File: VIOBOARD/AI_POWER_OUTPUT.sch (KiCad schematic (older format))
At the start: 17 parts, among them J5 24V OUTPUT

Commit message: Libraries modified as part of the BBB cape developement.
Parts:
- D24, D25, D26, D27, D28, D29, D30, D31: symbol device:D_ALT -> VIOBOARD-rescue:D_ALT-device
- R70, R71, R72, R73, R74, R75, R76, R77: symbol device:R -> VIOBOARD-rescue:R-device
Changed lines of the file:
@@
 	3150 4000 3450 4000
 $Comp
-L device:D_ALT D25
+L VIOBOARD-rescue:D_ALT-device D25
 U 1 1 599B8BEA
 P 6950 3600
@@
 $EndComp
 $Comp
-L device:D_ALT D24
+L VIOBOARD-rescue:D_ALT-device D24
 U 1 1 599B8BF2
 P 6950 3400
@@
 $EndComp
 $Comp
-L device:D_ALT D26
+L VIOBOARD-rescue:D_ALT-device D26
 U 1 1 599B9024
 P 6950 3800
@@
 $EndComp
 $Comp
-L device:D_ALT D27
+L VIOBOARD-rescue:D_ALT-device D27
 U 1 1 599B9072
 P 6950 4000
@@
 $EndComp
 $Comp
-L device:D_ALT D28
+L VIOBOARD-rescue:D_ALT-device D28
 U 1 1 599B90AF
 P 6950 4200
@@
 $EndComp
 $Comp
-L device:D_ALT D29
+L VIOBOARD-rescue:D_ALT-device D29
 U 1 1 599B90F1
 P 6950 4400
@@
 $EndComp
 $Comp
-L device:D_ALT D30
+L VIOBOARD-rescue:D_ALT-device D30
 U 1 1 599B9136
 P 6950 4600
@@
 $EndComp
 $Comp
-L device:D_ALT D31
+L VIOBOARD-rescue:D_ALT-device D31
 U 1 1 599B9184
 P 6950 4800
@@
 	7100 4800 8000 4800
 $Comp
-L device:R R70
+L VIOBOARD-rescue:R-device R70
 U 1 1 5A43596E
 P 8150 3400
@@
 $EndComp
 $Comp
-L device:R R71
+L VIOBOARD-rescue:R-device R71
 U 1 1 5A435AC5
 P 8150 3600
@@
 $EndComp
 $Comp
-L device:R R72
+L VIOBOARD-rescue:R-device R72
 U 1 1 5A435B1A
 P 8150 3800
@@
 $EndComp
 $Comp
-L device:R R73
+L VIOBOARD-rescue:R-device R73
 U 1 1 5A435B7A
 P 8150 4000
@@
 $EndComp
 $Comp
-L device:R R74
+L VIOBOARD-rescue:R-device R74
 U 1 1 5A435BDA
 P 8150 4200
@@
 $EndComp
 $Comp
-L device:R R75
+L VIOBOARD-rescue:R-device R75
 U 1 1 5A435C4C
 P 8150 4400
@@
 $EndComp
 $Comp
-L device:R R76
+L VIOBOARD-rescue:R-device R76
 U 1 1 5A435CFC
 P 8150 4600
@@
 $EndComp
 $Comp
-L device:R R77
+L VIOBOARD-rescue:R-device R77
 U 1 1 5A435D60
 P 8150 4800

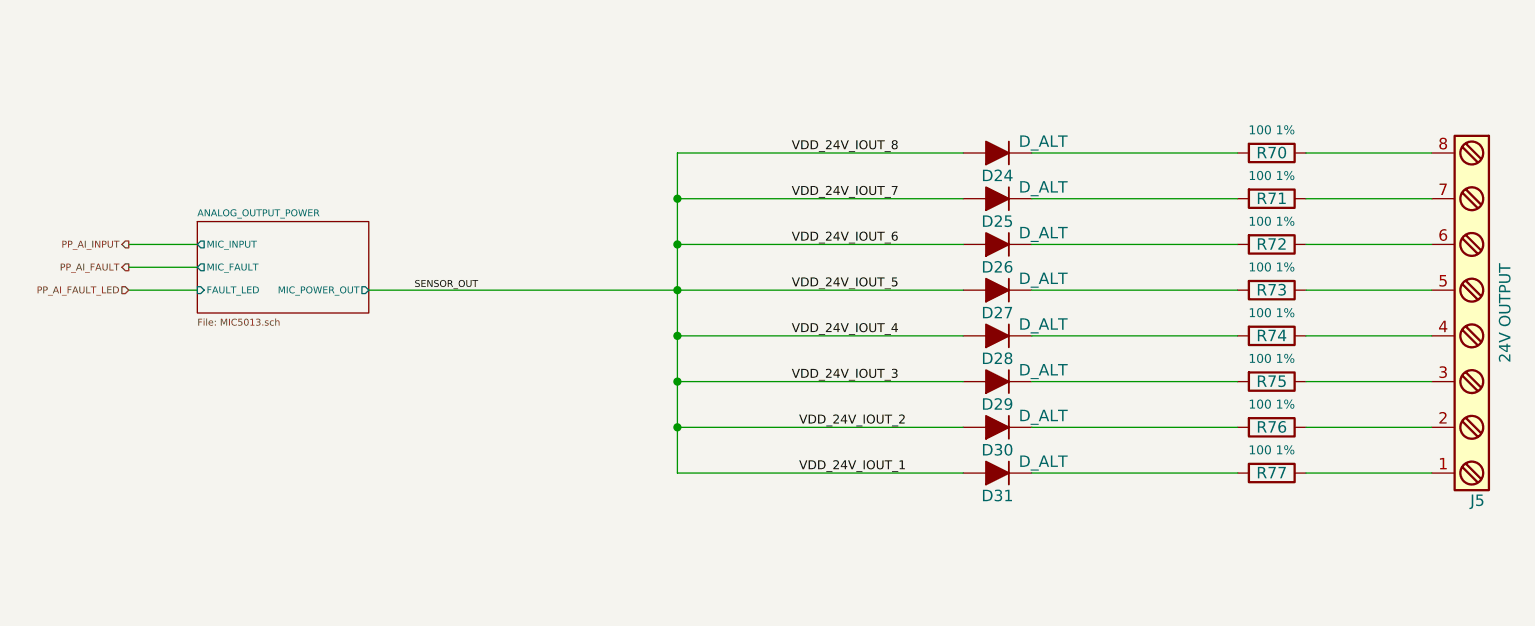
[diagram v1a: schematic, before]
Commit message: Schematics cleanup.  Gerbers for the latest manufacturing release.
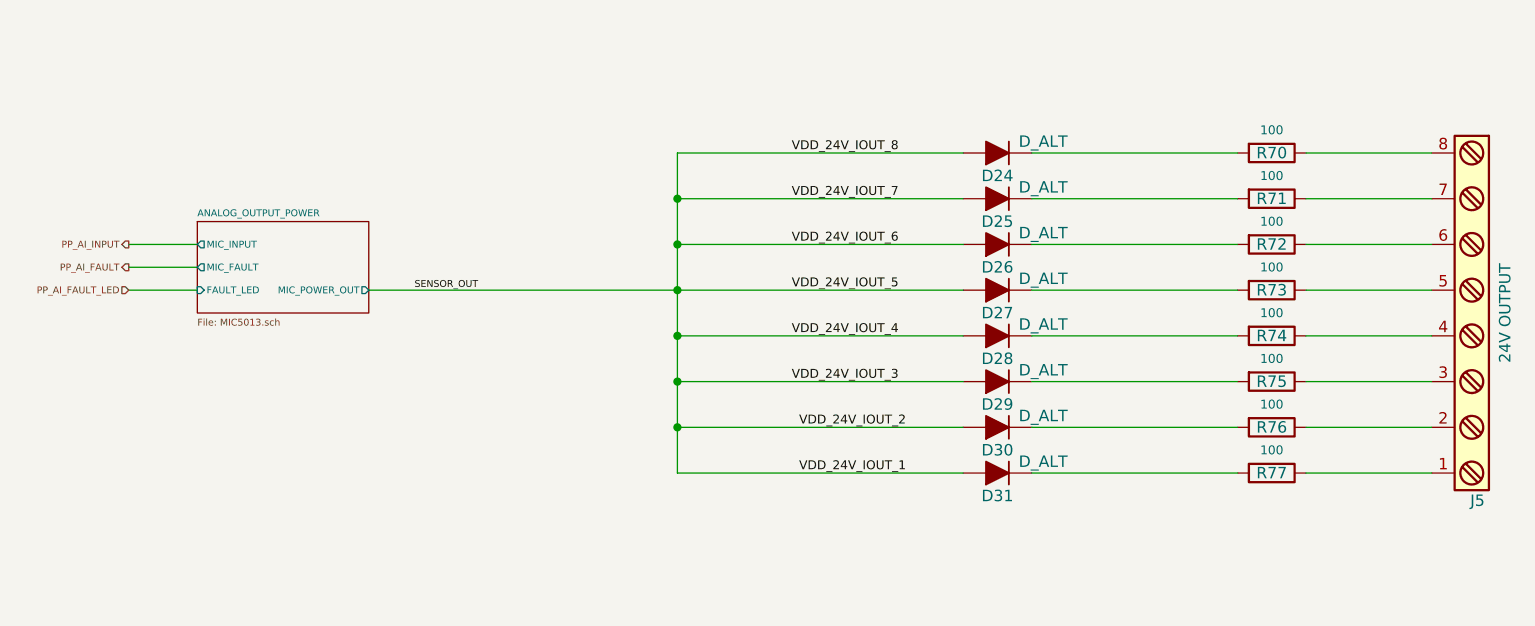
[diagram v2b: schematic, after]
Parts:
- R70, R71, R72, R73, R74, R75, R76, R77: value 100 1% -> 100
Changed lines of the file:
@@
 	5550 3800 6800 3800
 Wire Wire Line
-	4200 4000 6800 4000
+	4200 4000 5550 4000
 Wire Wire Line
 	5550 4400 6800 4400
@@
 	5550 3400 6800 3400
 Wire Wire Line
-	5550 3400 5550 4800
+	5550 3400 5550 3600
 Connection ~ 5550 3600
 Connection ~ 5550 3800
@@
 P 8150 3400
 F 0 "R70" V 8150 3400 50  0000 C CNN
-F 1 "100 1%" V 8050 3400 39  0000 C CNN
+F 1 "100" V 8050 3400 39  0000 C CNN
 F 2 "Resistors_SMD:R_0805" V 8080 3400 50  0001 C CNN
 F 3 "" H 8150 3400 50  0001 C CNN
@@
 P 8150 3600
 F 0 "R71" V 8150 3600 50  0000 C CNN
-F 1 "100 1%" V 8050 3600 39  0000 C CNN
+F 1 "100" V 8050 3600 39  0000 C CNN
 F 2 "Resistors_SMD:R_0805" V 8080 3600 50  0001 C CNN
 F 3 "" H 8150 3600 50  0001 C CNN
@@
 P 8150 3800
 F 0 "R72" V 8150 3800 50  0000 C CNN
-F 1 "100 1%" V 8050 3800 39  0000 C CNN
+F 1 "100" V 8050 3800 39  0000 C CNN
 F 2 "Resistors_SMD:R_0805" V 8080 3800 50  0001 C CNN
 F 3 "" H 8150 3800 50  0001 C CNN
@@
 P 8150 4000
 F 0 "R73" V 8150 4000 50  0000 C CNN
-F 1 "100 1%" V 8050 4000 39  0000 C CNN
+F 1 "100" V 8050 4000 39  0000 C CNN
 F 2 "Resistors_SMD:R_0805" V 8080 4000 50  0001 C CNN
 F 3 "" H 8150 4000 50  0001 C CNN
@@
 P 8150 4200
 F 0 "R74" V 8150 4200 50  0000 C CNN
-F 1 "100 1%" V 8050 4200 39  0000 C CNN
+F 1 "100" V 8050 4200 39  0000 C CNN
 F 2 "Resistors_SMD:R_0805" V 8080 4200 50  0001 C CNN
 F 3 "" H 8150 4200 50  0001 C CNN
@@
 P 8150 4400
 F 0 "R75" V 8150 4400 50  0000 C CNN
-F 1 "100 1%" V 8050 4400 39  0000 C CNN
+F 1 "100" V 8050 4400 39  0000 C CNN
 F 2 "Resistors_SMD:R_0805" V 8080 4400 50  0001 C CNN
 F 3 "" H 8150 4400 50  0001 C CNN
@@
 P 8150 4600
 F 0 "R76" V 8150 4600 50  0000 C CNN
-F 1 "100 1%" V 8050 4600 39  0000 C CNN
+F 1 "100" V 8050 4600 39  0000 C CNN
 F 2 "Resistors_SMD:R_0805" V 8080 4600 50  0001 C CNN
 F 3 "" H 8150 4600 50  0001 C CNN
@@
 P 8150 4800
 F 0 "R77" V 8150 4800 50  0000 C CNN
-F 1 "100 1%" V 8050 4800 39  0000 C CNN
+F 1 "100" V 8050 4800 39  0000 C CNN
 F 2 "Resistors_SMD:R_0805" V 8080 4800 50  0001 C CNN
 F 3 "" H 8150 4800 50  0001 C CNN
@@
 Wire Wire Line
 	8850 4800 8300 4800
+Wire Wire Line
+	5550 3600 5550 3800
+Wire Wire Line
+	5550 3800 5550 4000
+Wire Wire Line
+	5550 4000 6800 4000
+Wire Wire Line
+	5550 4000 5550 4200
+Wire Wire Line
+	5550 4200 5550 4400
+Wire Wire Line
+	5550 4400 5550 4600
+Wire Wire Line
+	5550 4600 5550 4800
 $EndSCHEMATC
